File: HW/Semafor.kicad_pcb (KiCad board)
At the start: 2 copper layers, 200 x 200 mm, 91 parts, among them J1 USB_C_Receptacle_USB2.0, J2 USB_plug, M1 Motor_DC, Q1 Q_NMOS_GSD, Q3 Q_NMOS_GSD, Q4 Q_NMOS_GSD, SW6 SW_SPDT, U1 ESP32-C3, U2 CN3058E, U3 LT1930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

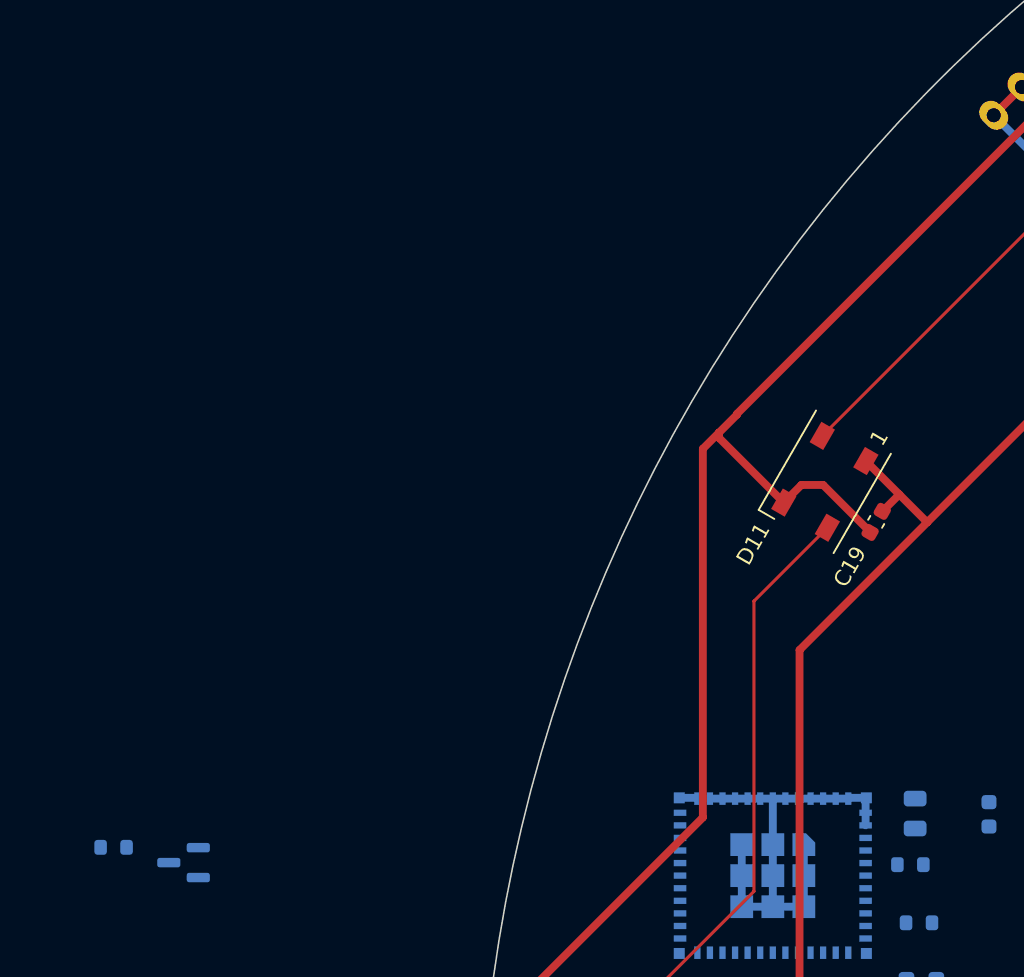
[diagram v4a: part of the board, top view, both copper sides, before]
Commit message: repair mistakes in schematic, add switched supply voltage to LoRa, LEDs and converter for capacitive buttons
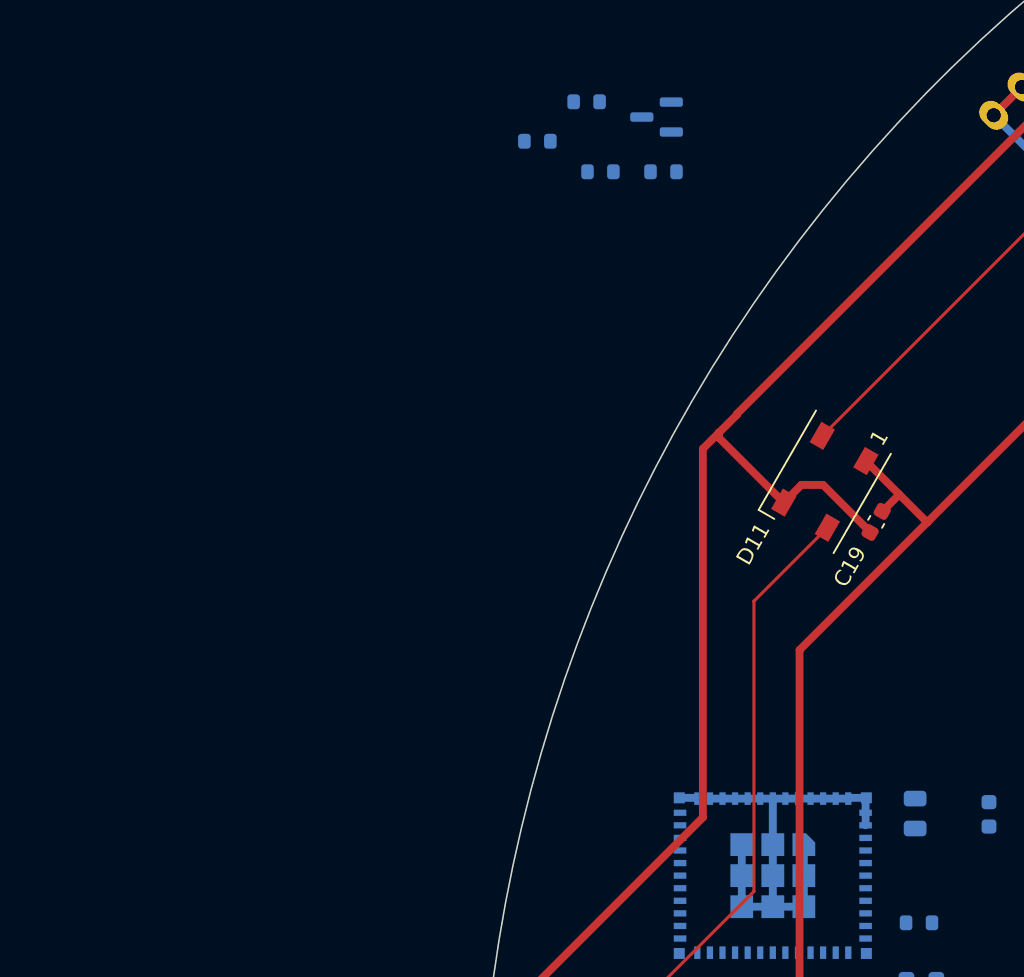
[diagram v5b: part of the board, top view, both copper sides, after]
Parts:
- removed U6: CJ431, Package_TO_SOT_SMD:SOT-23
- added Q2: Q_NMOS_GSD, Package_TO_SOT_SMD:SOT-23, B.Cu at (-188.7, -168.3)
- added R24: 10k, Resistor_SMD:R_0603_1608Metric, B.Cu at (-192.3, -164.9)
- added R25: 100k, Resistor_SMD:R_0603_1608Metric, B.Cu at (-196.3, -166.8)
- R1: value 10k -> 47k
- moved R1 55.4 mm to (-188.3, -164.9)
- moved R7 52.7 mm to (-193.1, -169.3)
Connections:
- BT1 pad 1: Net-(BT1-Pad1) -> Net-(C10-Pad1)
- C10 pad 1: +3V3 -> Net-(C10-Pad1)
- C13 pad 1: +3V3 -> 3V3_SWITCHED
- C3 pad 1: +3V3 -> 3V3_SWITCHED
- C4 pad 1: +3V3 -> 3V3_SWITCHED
- L1 pad 1: +3V3 -> 3V3_SWITCHED
- R13 pad 1: +3V3 -> 3V3_SWITCHED
- R16 pad 1: +3V3 -> 3V3_SWITCHED
- R17 pad 1: +3V3 -> 3V3_SWITCHED
- R18 pad 1: +3V3 -> 3V3_SWITCHED
- R7 pad 1: +3V3 -> U_BAT_ADC
- R7 pad 2: Net-(R7-Pad2) -> GND
- SW6 pad 2: Net-(BT1-Pad1) -> Net-(C10-Pad1)
- U1 pad 18: unconnected-(U1-Pad18) -> U_BAT_ADC
- U1 pad 19: unconnected-(U1-Pad19) -> Net-(U1-Pad19)
- U1 pad 20: unconnected-(U1-Pad20) -> MOTOR
- U1 pad 21: unconnected-(U1-Pad21) -> PIEZO
- U1 pad 22: unconnected-(U1-Pad22) -> SCL
- U1 pad 23: unconnected-(U1-Pad23) -> SDA
- U1 pad 5: Net-(R7-Pad2) -> Net-(U1-Pad5)
- U1 pad 6: unconnected-(U1-Pad6) -> CHANGE_OF_CAP_BUT
- U2 pad 1: unconnected-(U2-Pad1) -> GND
- U2 pad 5: +3V3 -> Net-(C10-Pad1)
- U2 pad 8: +3V3 -> Net-(C10-Pad1)
- U3 pad 5: +3V3 -> 3V3_SWITCHED
- U4 pad 6: +3V3 -> 3V3_SWITCHED
- U5 pad 1: +3V3 -> 3V3_SWITCHED
- U5 pad 5: unconnected-(U5-Pad5) -> CHANGE_OF_CAP_BUT

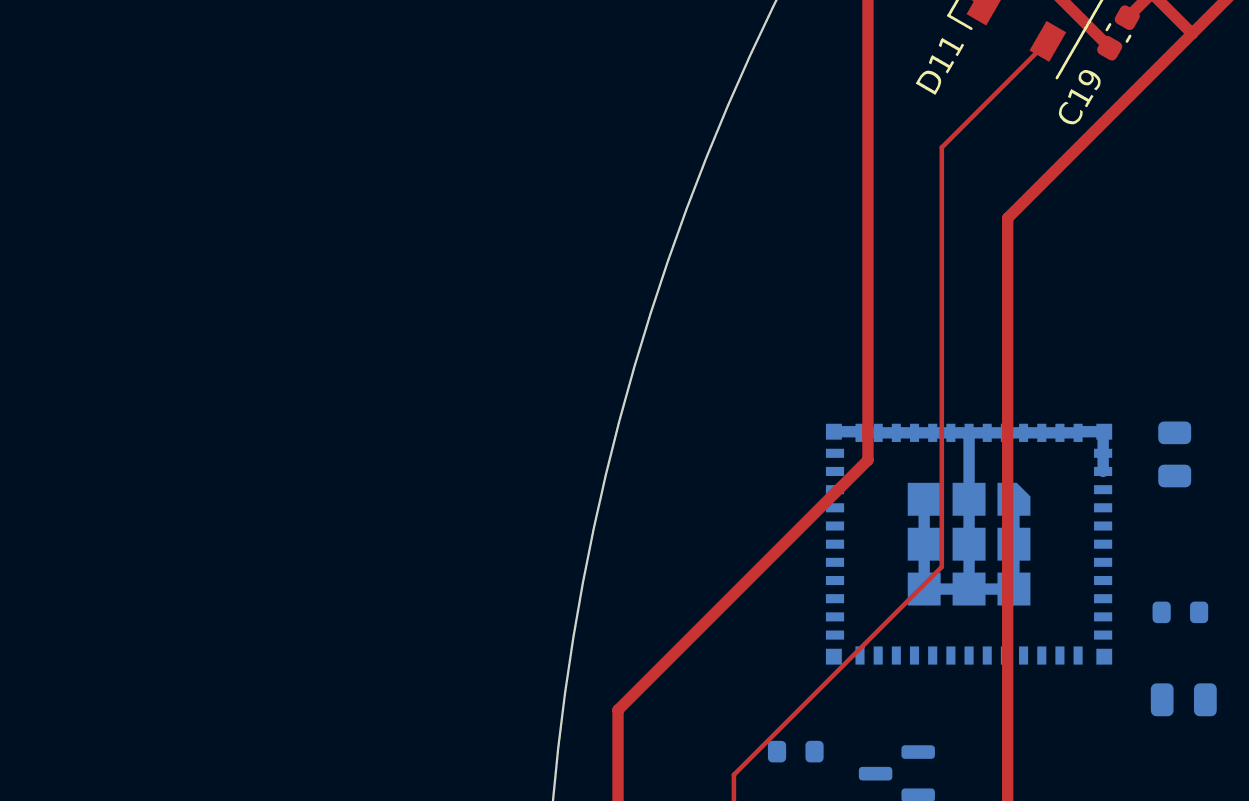
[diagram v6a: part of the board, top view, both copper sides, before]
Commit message: repair ERC errors
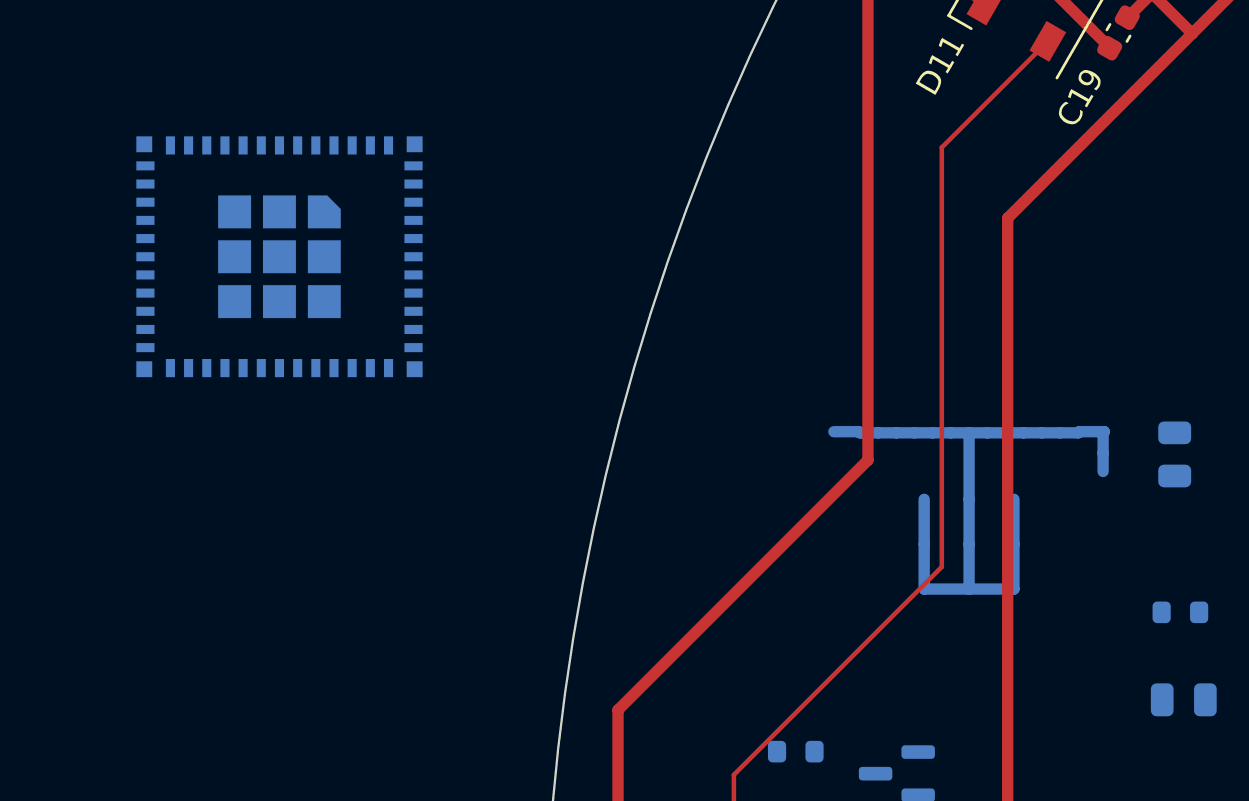
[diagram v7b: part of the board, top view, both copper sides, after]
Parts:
- moved U1 32.9 mm to (-211.7, -132.8)

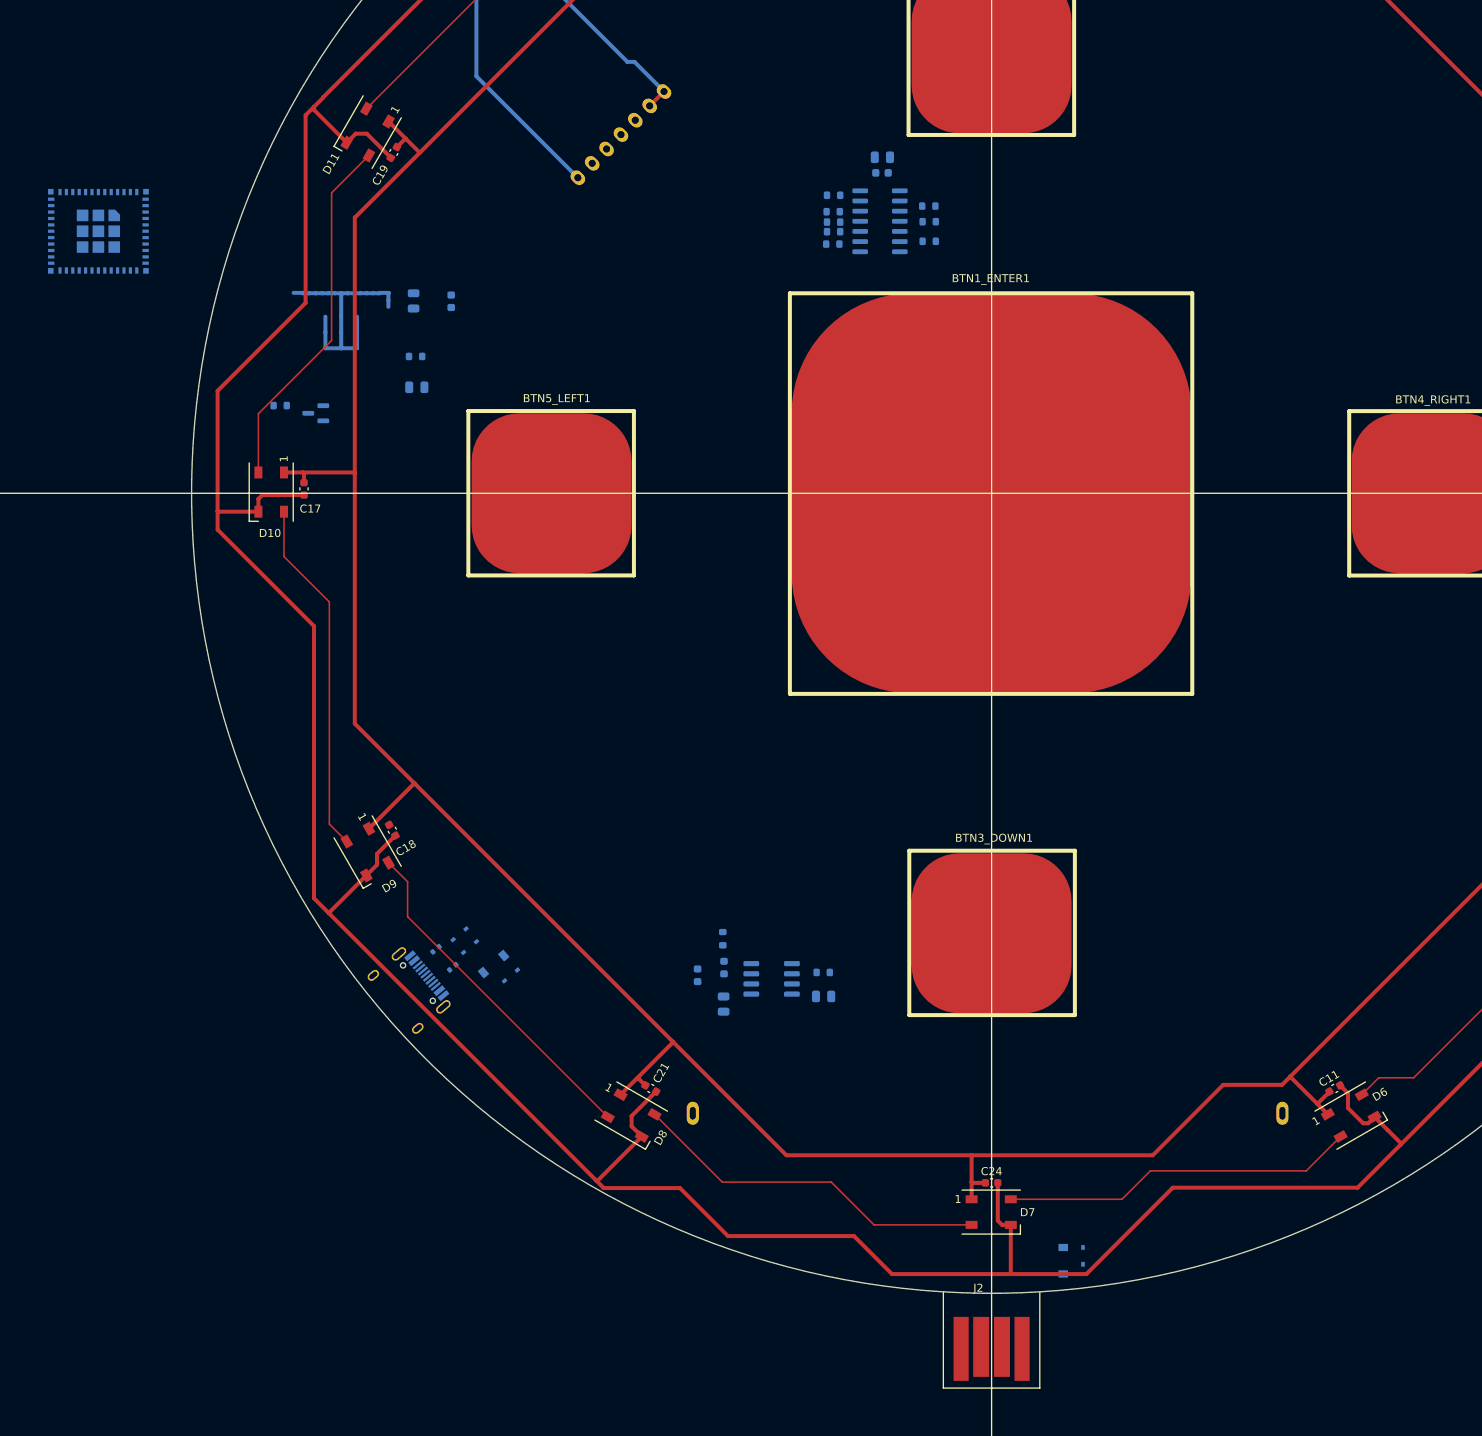
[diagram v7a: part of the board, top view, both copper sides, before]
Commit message: routing ESP and charger
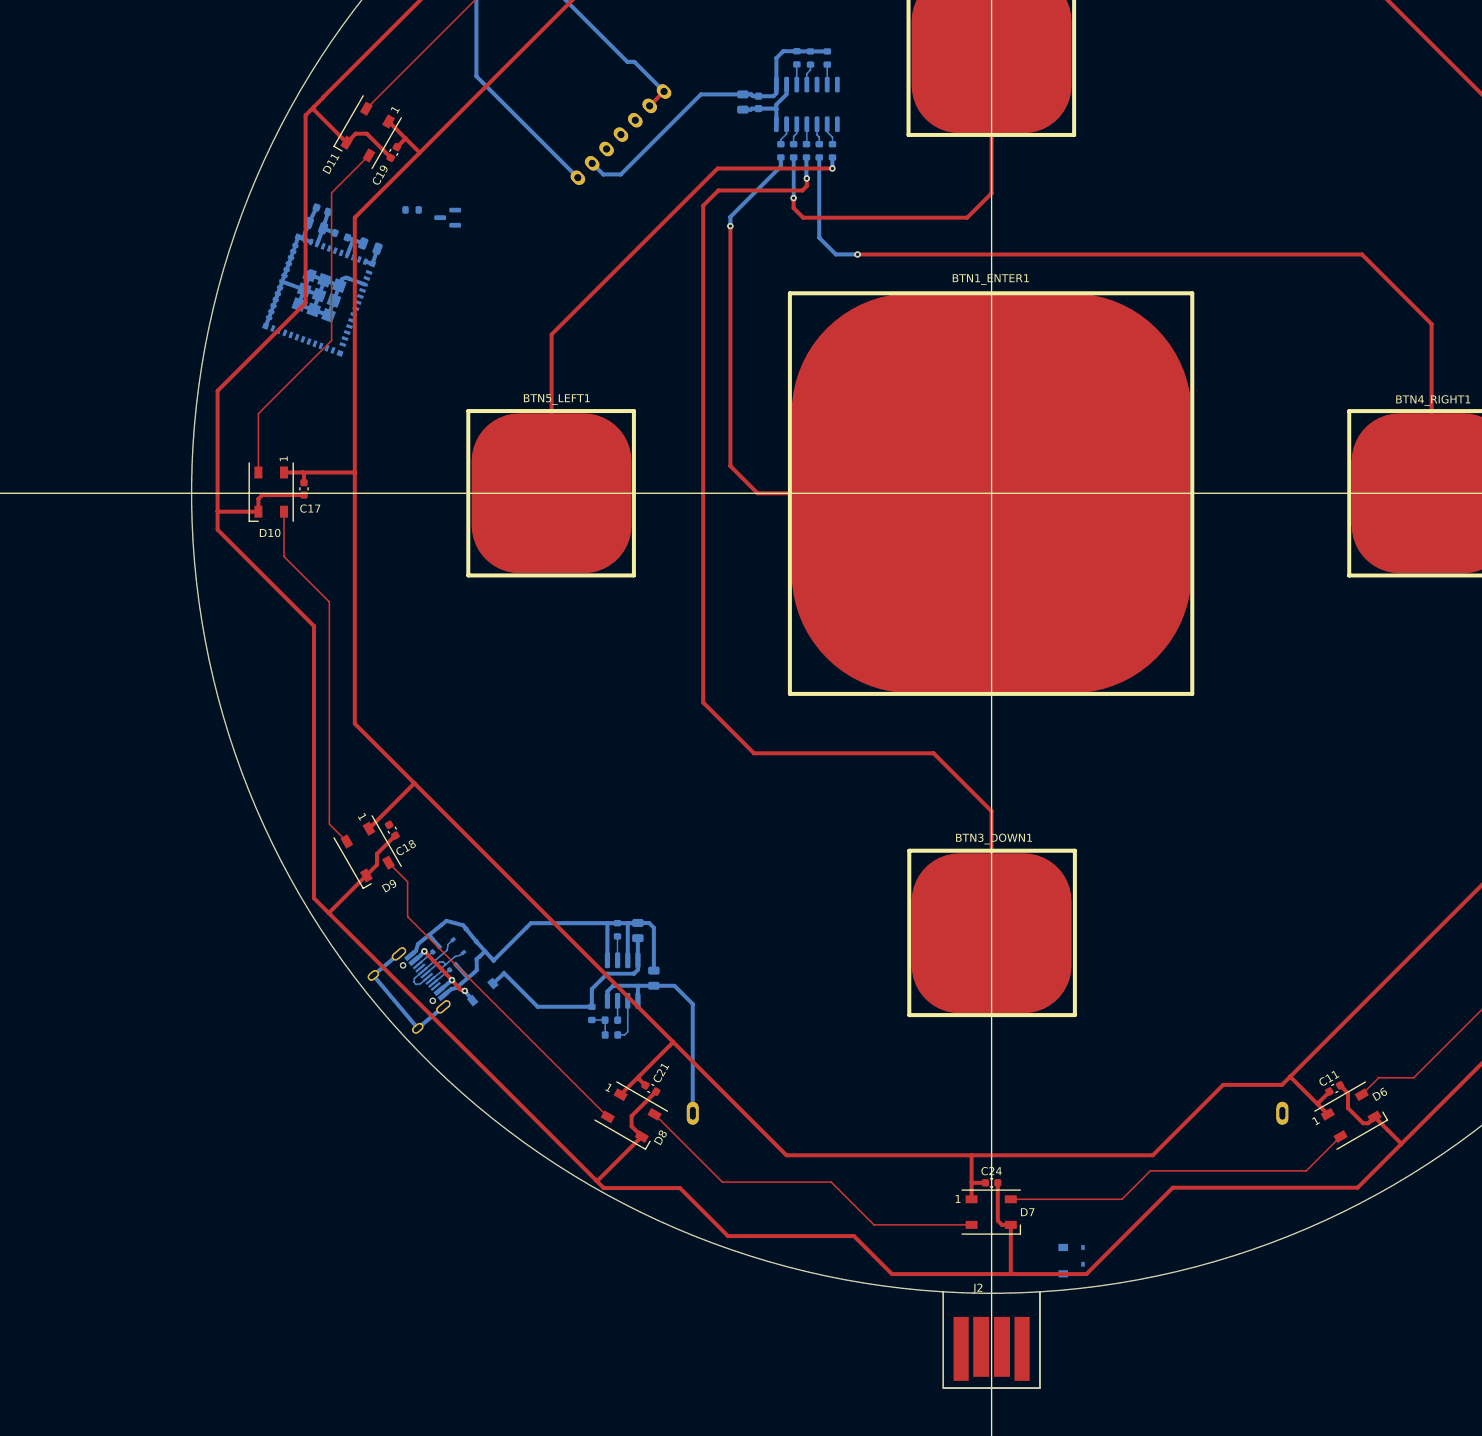
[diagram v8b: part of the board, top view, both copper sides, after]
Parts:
- moved Q1 29.5 mm to (-168.0, -134.4)
- moved R4 29.5 mm to (-172.4, -135.4)
- moved U1 28.7 mm to (-184.1, -124.8), turned to -110 degrees
- moved R8 26.3 mm to (-146.8, -45.4), turned to 90 degrees
- moved R18 26.2 mm to (-120.5, -154.4), turned to -90 degrees
- moved R16 25.3 mm to (-122.6, -154.4), turned to -90 degrees
- moved R17 24.8 mm to (-124.3, -154.4), turned to -90 degrees
- moved C1 24.6 mm to (-144.2, -45.3), turned to 90 degrees
- moved C9 19.8 mm to (-183.7, -135.4), turned to 160 degrees
- moved R6 18.8 mm to (-150.0, -35.0)
- moved C3 18.8 mm to (-131.1, -148.9), turned to -90 degrees
- moved U2 18.6 mm to (-146.1, -39.1), turned to -90 degrees
- moved C2 18.6 mm to (-177.7, -130.9), turned to -20 degrees
- moved R5 17.8 mm to (-181.3, -132.2), turned to -20 degrees
- moved C4 17.8 mm to (-129.1, -148.9), turned to -90 degrees
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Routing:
- net Net-(BTN3_DOWN1-Pad1): track 0.00 -> 136.6 mm, vias 0 -> 1
- net Net-(BTN4_RIGHT1-Pad1): track 0.00 -> 112.2 mm, vias 0 -> 1
- net GND: track 839.2 -> 929.4 mm
- net Net-(BTN1_ENTER1-Pad1): track 0.00 -> 75.3 mm, vias 0 -> 1
- net Net-(BTN5_LEFT1-Pad1): track 0.00 -> 64.9 mm, vias 0 -> 1
- net Net-(BTN2_UP1-Pad1): track 0.00 -> 50.3 mm, vias 0 -> 1
- net 3V3_SWITCHED: track 0.00 -> 39.1 mm
- net Net-(BT1-Pad1): track 0.00 -> 28.6 mm
- net +5V: track 0.00 -> 27.5 mm
- net unconnected-(J1-PadS1): track 0.00 -> 17.0 mm
- net Net-(D24-Pad2): track 0.00 -> 12.5 mm, vias 0 -> 3
- net D+: track 0.00 -> 9.67 mm
- net D-: track 0.00 -> 8.78 mm
- net +3V3: track 0.00 -> 5.87 mm
- net Net-(D13-Pad1): track 0.00 -> 5.28 mm
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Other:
- board size 200 x 200 mm -> 200 x 211.8 mm
